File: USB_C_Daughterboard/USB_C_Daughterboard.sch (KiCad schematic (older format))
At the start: 11 parts, among them J1 USB_C_Receptacle_USB2.0

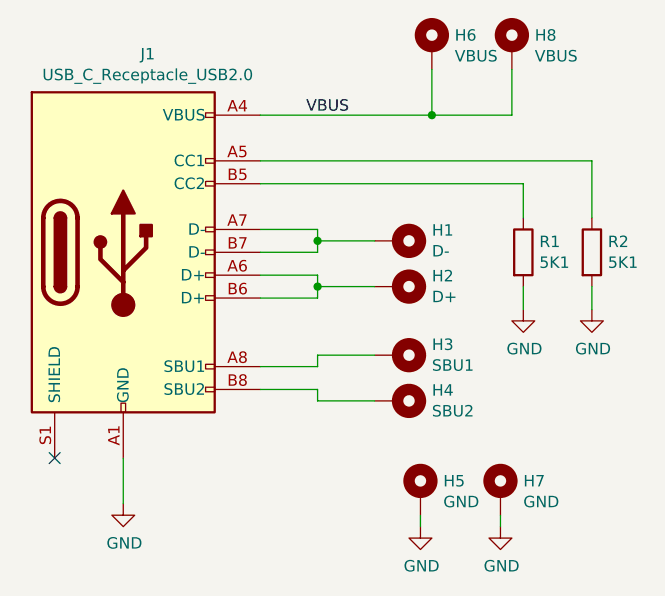
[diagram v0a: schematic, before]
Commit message: Rename daughterboard nets for better PCBnew labeling
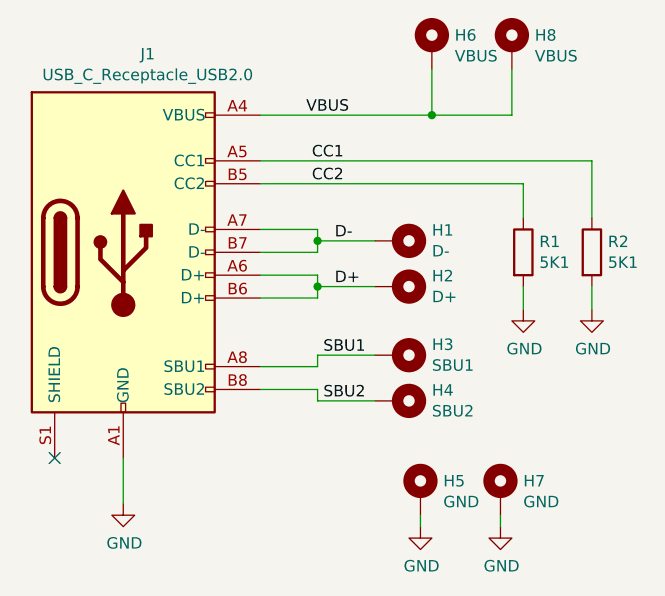
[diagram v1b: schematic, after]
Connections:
- net CC1: now reaches J1.A5 (CC1), R2.1
- net D+: now reaches H2.1, J1.A6 (D+), J1.B6 (D+)
- net D-: now reaches H1.1, J1.A7 (D-), J1.B7 (D-)
- net SBU1: now reaches H3.1, J1.A8 (SBU1)
- net CC2: now reaches J1.B5 (CC2), R1.1
- net SBU2: now reaches H4.1, J1.B8 (SBU2)
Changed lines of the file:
@@
 Text Label 4950 3150 0    50   ~ 0
 VBUS
+Text Label 5075 3700 0    50   ~ 0
+D-
+Text Label 5075 3900 0    50   ~ 0
+D+
+Text Label 5025 4200 0    50   ~ 0
+SBU1
+Text Label 5025 4400 0    50   ~ 0
+SBU2
+Text Label 4975 3350 0    50   ~ 0
+CC1
+Text Label 4975 3450 0    50   ~ 0
+CC2
 $EndSCHEMATC
